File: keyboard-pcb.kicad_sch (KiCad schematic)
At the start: 0 parts

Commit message: added stm32
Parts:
- added D1: PRTR5V0U2X, Package_TO_SOT_SMD:SOT-143, symbol Power_Protection:PRTR5V0U2X
- added J1: USB_C_Receptacle_USB2.0_14P, symbol Connector:USB_C_Receptacle_USB2.0_14P
- added R1, R2: 5.1k, symbol Device:R_Small_US
- added U1: STM32F072CBTx, Package_QFP:LQFP-48_7x7mm_P0.5mm, symbol MCU_ST_STM32F0:STM32F072CBTx
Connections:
- new net: J1.A4 (VBUS), J1.A9 (VBUS), J1.B4 (VBUS), J1.B9 (VBUS)
- new net: J1.A5 (CC1), R2.1
- new net: J1.B5 (CC2), R1.2
- new net +3V3: U1.1 (VBAT), U1.24 (VDD), U1.36 (VDDIO2), U1.48 (VDD), U1.9 (VDDA)
- new net GND: J1.A1 (GND), J1.A12 (GND), J1.B1 (GND), J1.B12 (GND), J1.SH (SHIELD), R1.1, R2.2, U1.23 (VSS), U1.35 (VSS), U1.47 (VSS), U1.8 (VSSA)
- new net USB_D+: J1.A6 (D+), J1.B6 (D+), U1.33 (PA12)
- new net USB_D-: J1.A7 (D-), J1.B7 (D-), U1.32 (PA11)

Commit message: added libraries
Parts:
- removed D1: PRTR5V0U2X, Package_TO_SOT_SMD:SOT-143, symbol Power_Protection:PRTR5V0U2X
- added C1, C2, C3, C4, C5: 0.1uF, symbol Device:C_Small
- added C6, C7, C8: 1uF, symbol Device:C_Small
- added D1: D5V0F1U2LP-7B, Diode_SMD:D_0402_1005Metric_Pad0.77x0.64mm_HandSolder, symbol Device:D_TVS
- added D2: PRTR5V0U2X, Package_TO_SOT_SMD:SOT-143, symbol Power_Protection:PRTR5V0U2X
- added D4: BZT52C5V1-7-F, Diode_SMD:D_SOD-123, symbol Device:D_Zener
- added U2: XC6206PxxxMR, Package_TO_SOT_SMD:SOT-23-3, symbol Regulator_Linear:XC6206PxxxMR
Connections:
- net +3V3: now also C1.1, C2.1, C3.1, C4.1, C5.1, C6.1, C8.1, U2.2 (VO)
- net GND: now also C1.2, C2.2, C3.2, C4.2, C5.2, C6.2, C7.2, C8.2, D1.1 (A1), D2.1 (GND), U2.1 (GND)
- net at J1.A4 (VBUS), J1.A9 (VBUS), J1.B4 (VBUS)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: now also D1.2 (A2), D4.2 (A)
- net USB_D+ renamed D+
- net D+: now also D2.3 (I/O2)
- net USB_D- renamed D-
- net D-: now also D2.2 (I/O1)
- new net +5V: C7.1, D2.4 (VCC), D4.1 (K), U2.3 (VI)
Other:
- note added: "Decoupling Capacitors"
- note added: "MCU"
- note added: "USB Port"
- moved on the sheet: J1, R1, R2

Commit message: finished rest of the schematic
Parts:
- removed D1: D5V0F1U2LP-7B, Diode_SMD:D_0402_1005Metric_Pad0.77x0.64mm_HandSolder, symbol Device:D_TVS
- removed D4: BZT52C5V1-7-F, Diode_SMD:D_SOD-123, symbol Device:D_Zener
- added C9: 0.1uF, symbol Device:C_Small
- added F1: 500mA, symbol Device:Polyfuse
- added J4: Conn_01x05, symbol Connector_Generic:Conn_01x05
- added R3, R4: 5.1k, symbol Device:R_Small_US
- added SW1, SW2: RESET, symbol Switch:SW_Push
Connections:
- net +3V3: now also J4.5 (Pin_5), SW2.1
- net +5V: now also F1.2; no longer D2.4 (VCC)
- net GND: now also C9.2, J4.1 (Pin_1), R4.1, SW1.2
- net VBUS: now reaches J1.A4 (VBUS), J1.A9 (VBUS), J1.B4 (VBUS), J1.B9 (VBUS)
- net VBUS: now also D2.4 (VCC), F1.1
- net CLK: now reaches U1.34 (PA13)
- net DATA: now reaches U1.37 (PA14)
- net BOOT: now reaches U1.44 (BOOT0)
- net BOOT: now also R3.2, SW2.2
- net NRST: now reaches U1.7 (NRST)
- net NRST: now also C9.1, SW1.1
- new net: R3.1, R4.2
- new net RST: J4.4 (Pin_4)
- new net SWCLK: J4.3 (Pin_3)
- new net SWDIO: J4.2 (Pin_2)
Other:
- added sheet Keyboard Matrix (keyboard-matrix.kicad_sch)
- note added: "Boot and Reset switches"
- note added: "Debug"
- note added: "ESD Protection"
- note added: "LDO"
- note added: "USB-C Port"
- note removed: "USB Port"
- title: (none) -> AwesomeKey
- moved on the sheet: C1, C2, C3, C4, C5, C6, C7, C8, D2, J1, R1, R2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

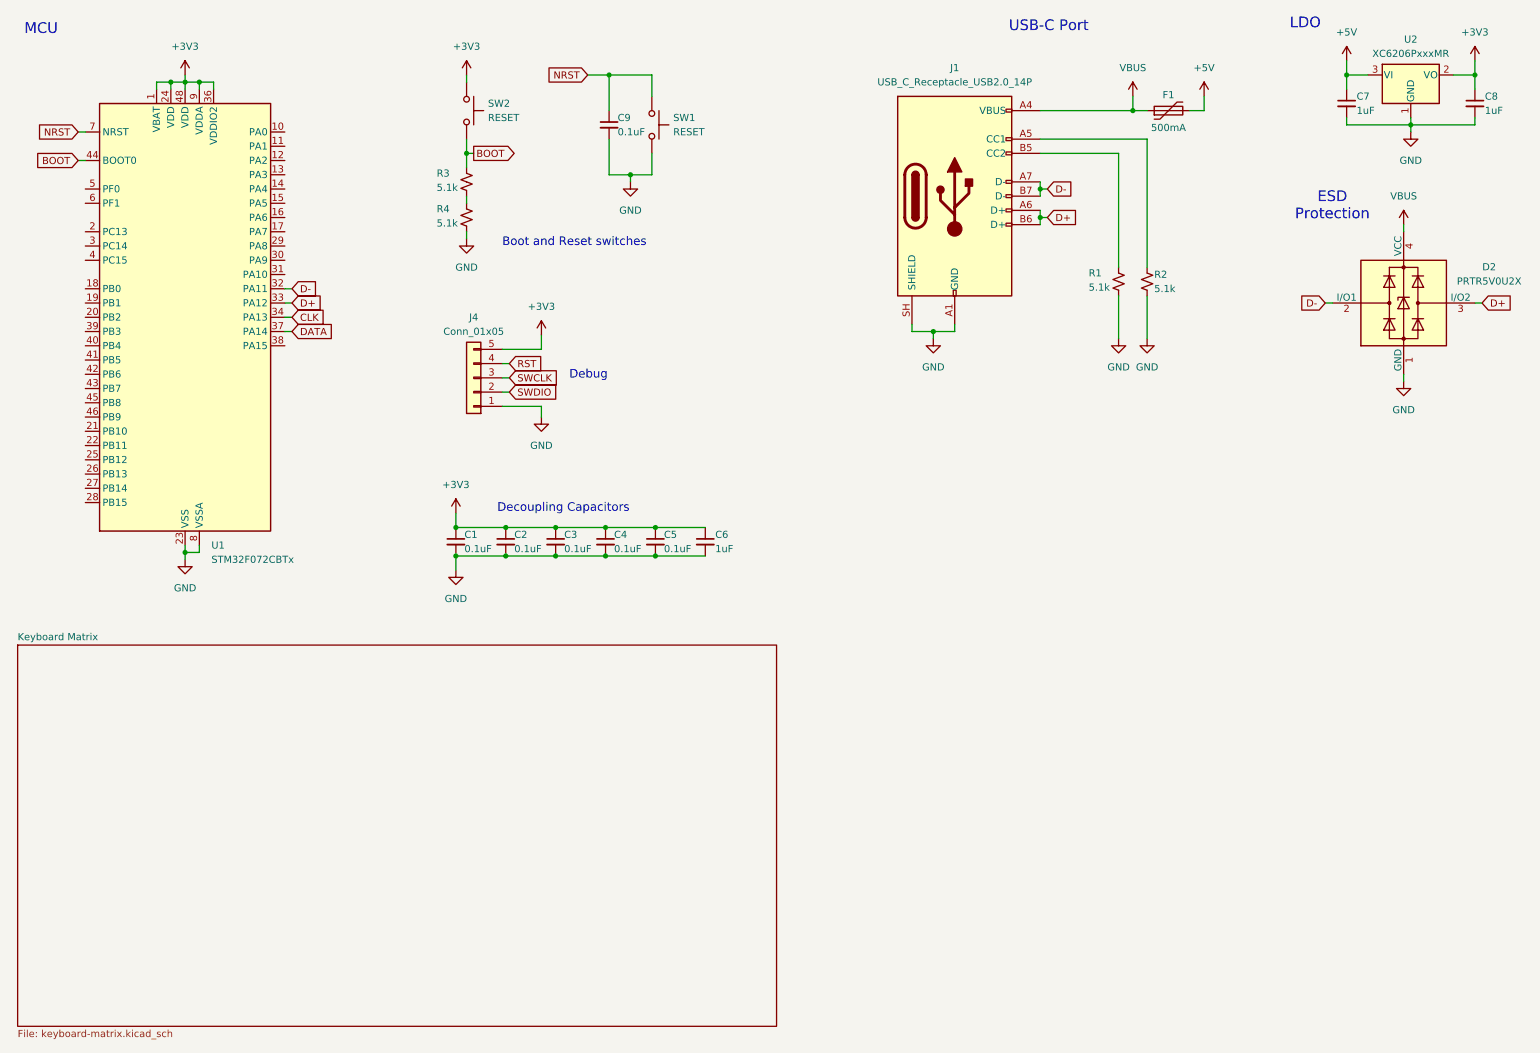
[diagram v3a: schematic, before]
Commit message: added led matrix for backlight
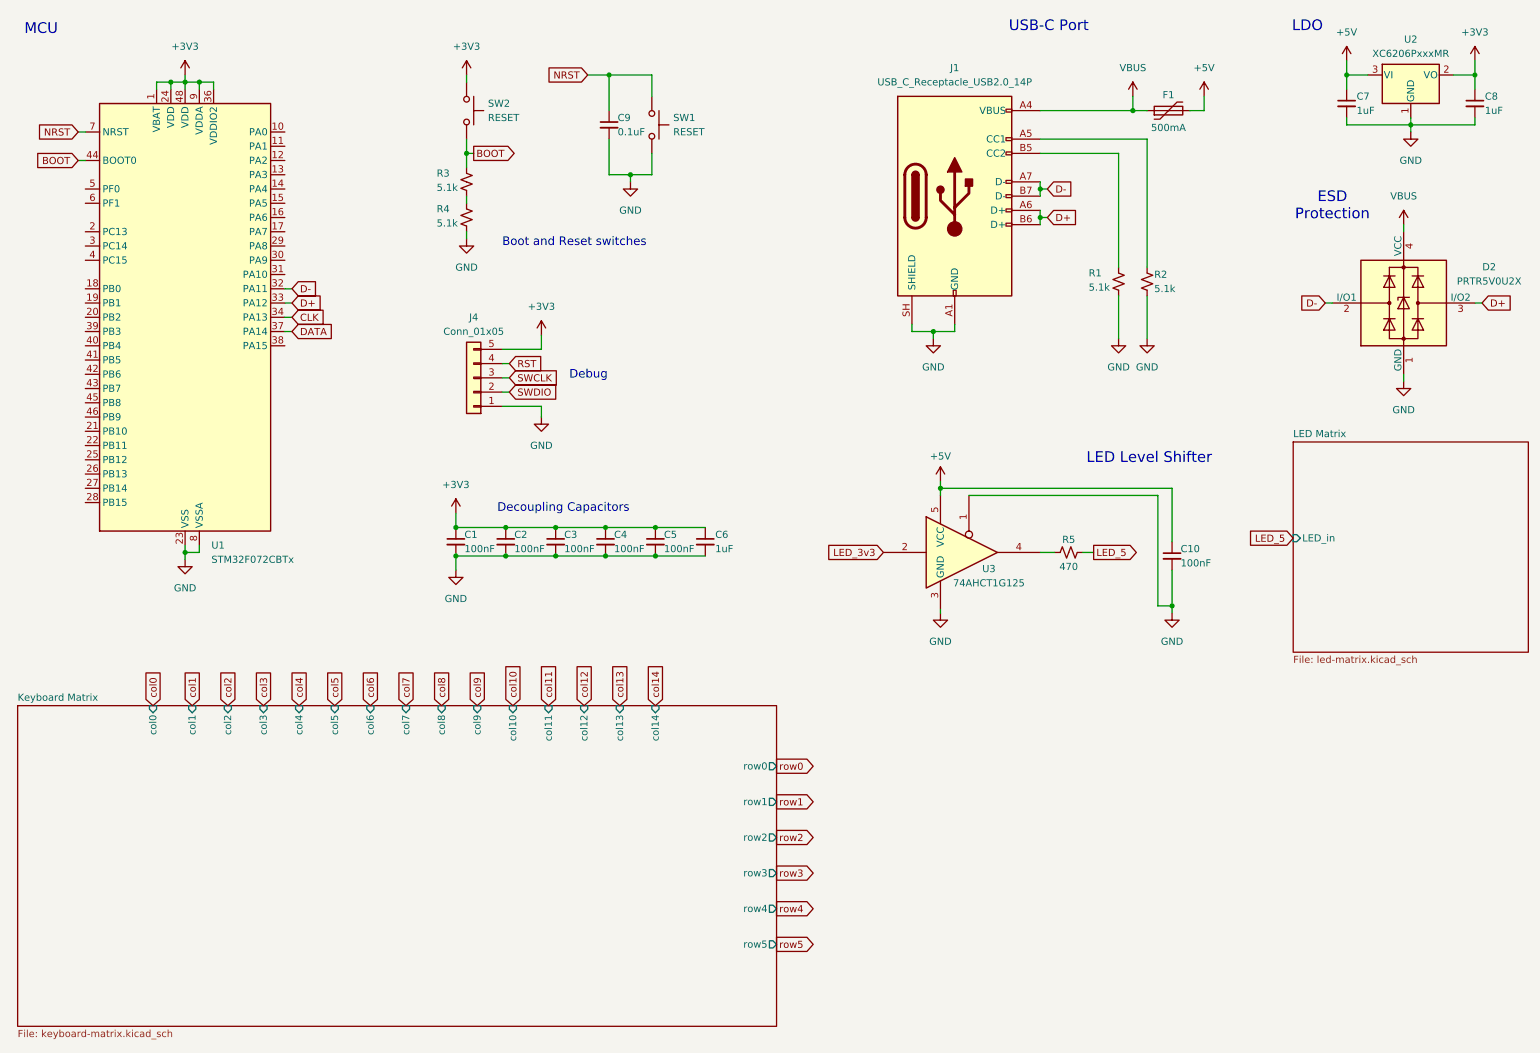
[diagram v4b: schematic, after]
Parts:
- added C10: 100nF, symbol Device:C_Small
- added R5: 470, symbol Device:R_Small_US
- added U3: 74AHCT1G125, symbol 74xGxx:74AHCT1G125
- C1, C2, C3, C4, C5: value 0.1uF -> 100nF
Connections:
- net +5V: now also C10.1, U3.5 (VCC)
- net GND: now also C10.2, U3.1, U3.3 (GND)
- new net: R5.1, U3.4
- new net LED_3v3: U3.2
- new net LED_5: R5.2
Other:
- added sheet LED Matrix (led-matrix.kicad_sch)
- sheet Keyboard Matrix ports: added col0, col1, col10, col11, col12, col13, col14, col2, col3, col4, col5, col6, col7, col8, col9, row0, row1, row2, row3, row4, row5; removed none
- note added: "LED Level Shifter"

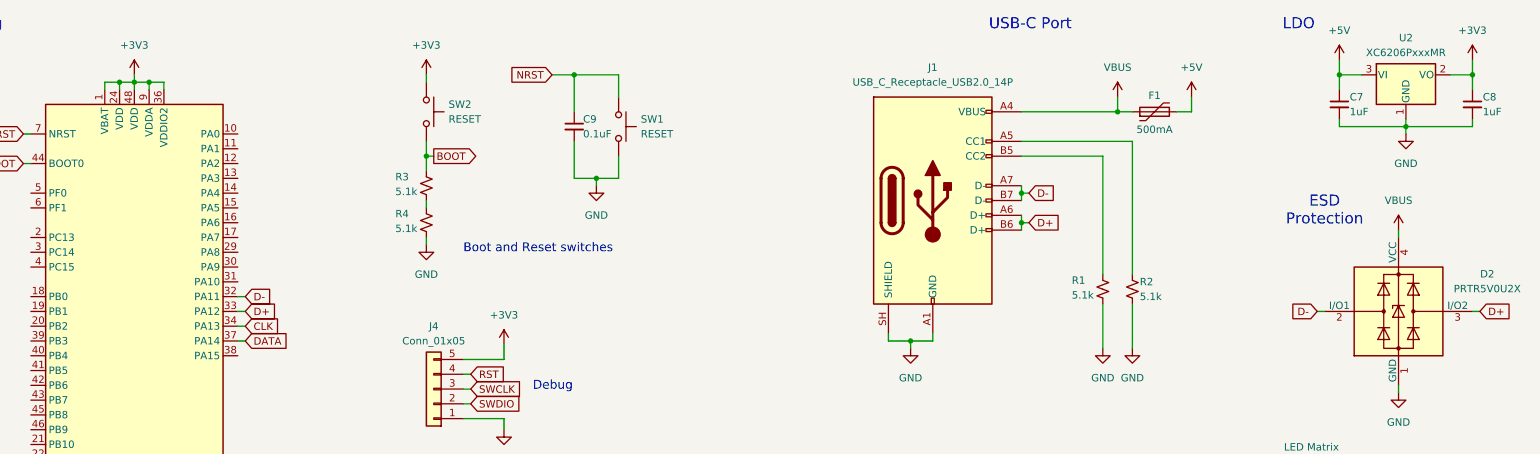
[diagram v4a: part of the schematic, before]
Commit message: assigned footprints
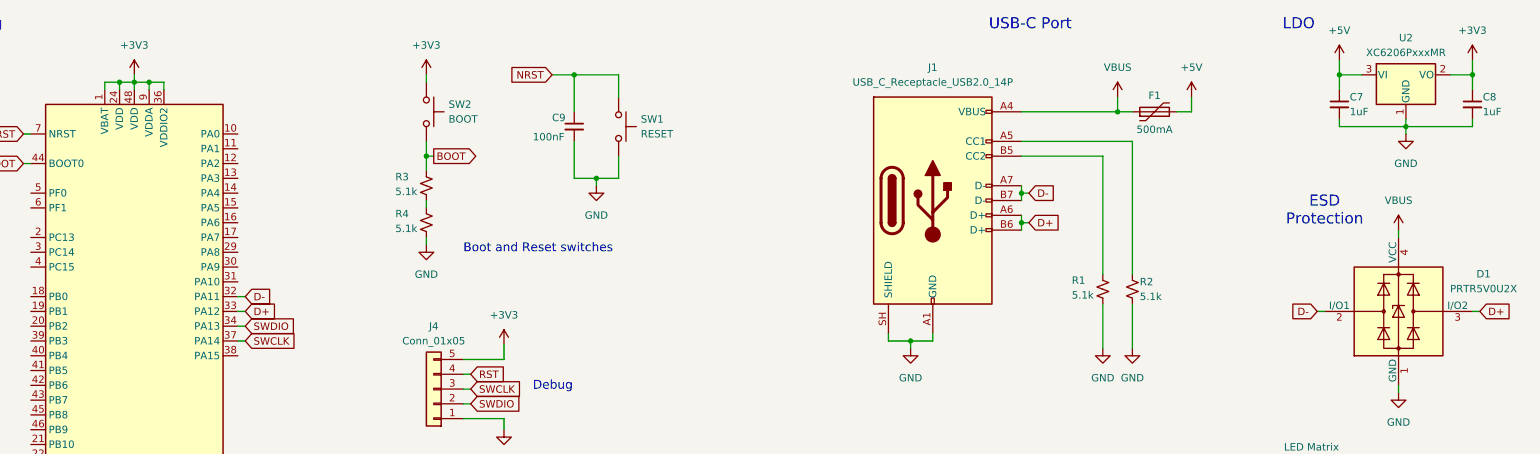
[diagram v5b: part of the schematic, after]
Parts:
- C1, C10, C2, C3, C4, C5: footprint (none) -> Capacitor_SMD:C_0402_1005Metric
- C6, C7, C8: footprint (none) -> Capacitor_SMD:C_0603_1608Metric
- C9: value 0.1uF -> 100nF; footprint (none) -> Capacitor_SMD:C_0402_1005Metric
- F1: footprint (none) -> Fuse:Fuse_1206_3216Metric
- J1: footprint (none) -> PCM_marbastlib-various:USB_C_Receptacle_HRO_TYPE-C-31-M-12
- J4: footprint (none) -> Connector_PinHeader_2.54mm:PinHeader_1x05_P2.54mm_Vertical
- R1, R2, R3, R4, R5: footprint (none) -> Resistor_SMD:R_0402_1005Metric
- SW1: footprint (none) -> Button_Switch_SMD:SW_SPST_TL3342
- SW2: value RESET -> BOOT; footprint (none) -> Button_Switch_SMD:SW_SPST_TL3342
- U3: footprint (none) -> Package_TO_SOT_SMD:SOT-23-5
- renumbered D2 to D1
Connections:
- net CLK is gone; now on net SWDIO: U1.34 (PA13)
- net DATA is gone; now on net SWCLK: U1.37 (PA14)
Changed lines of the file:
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@@
 	)
 	(junction
-		(at 41.275 26.67)
-		(diameter 0)
-		(color 0 0 0 0)
-	)
-	(junction
 		(at 177.165 71.12)
 		(diameter 0)
@@
 	)
 	(junction
+		(at 41.275 26.67)
+		(diameter 0)
+		(color 0 0 0 0)
+	)
+	(junction
 		(at 127.635 106.045)
 		(diameter 0)
@@
 	(wire
 		(pts
+			(xy 38.735 26.67) (xy 38.735 27.94)
+		)
+		(stroke
+			(width 0)
+			(type default)
+		)
+	)
+	(wire
+		(pts
 			(xy 93.98 39.37) (xy 95.25 39.37)
 		)
@@
 	(wire
 		(pts
-			(xy 38.735 27.94) (xy 38.735 26.67)
-		)
-		(stroke
-			(width 0)
-			(type default)
-		)
-	)
-	(wire
-		(pts
 			(xy 48.895 26.67) (xy 46.355 26.67)
 		)
@@
 		)
 	)
-	(global_label "CLK"
+	(global_label "SWCLK"
 		(shape input)
-		(at 62.865 68.58 0)
+		(at 62.865 71.12 0)
 		(fields_autoplaced yes)
 		(effects
@@
 		)
 		(property "Intersheetrefs" "${INTERSHEET_REFS}"
-			(at 69.4183 68.58 0)
+			(at 72.0792 71.12 0)
 			(hide yes)
 			(show_name no)
@@
 		)
 	)
-	(global_label "DATA"
+	(global_label "SWDIO"
 		(shape input)
-		(at 62.865 71.12 0)
+		(at 62.865 68.58 0)
 		(fields_autoplaced yes)
 		(effects
@@
 		)
 		(property "Intersheetrefs" "${INTERSHEET_REFS}"
-			(at 70.265 71.12 0)
+			(at 71.7164 68.58 0)
 			(hide yes)
 			(show_name no)
@@
 			)
 		)
-		(property "Footprint" ""
+		(property "Footprint" "PCM_marbastlib-various:USB_C_Receptacle_HRO_TYPE-C-31-M-12"
 			(at 184.785 46.99 0)
 			(hide yes)
@@
 			)
 		)
-		(property "Footprint" ""
+		(property "Footprint" "Resistor_SMD:R_0402_1005Metric"
 			(at 215.265 62.23 0)
 			(hide yes)
@@
 			)
 		)
-		(property "Footprint" ""
+		(property "Footprint" "Capacitor_SMD:C_0603_1608Metric"
 			(at 250.825 30.48 0)
 			(hide yes)
@@
 		(dnp no)
 		(property "Reference" "C9"
-			(at 120.904 33.02 0)
+			(at 115.57 32.766 0)
 			(show_name no)
 			(do_not_autoplace no)
@@
 			)
 		)
-		(property "Value" "0.1uF"
-			(at 120.904 35.56 0)
+		(property "Value" "100nF"
+			(at 112.268 36.068 0)
 			(show_name no)
 			(do_not_autoplace no)
@@
 			)
 		)
-		(property "Footprint" ""
+		(property "Footprint" "Capacitor_SMD:C_0402_1005Metric"
 			(at 119.38 34.29 0)
 			(hide yes)
@@
 			)
 		)
-		(property "Value" "RESET"
+		(property "Value" "BOOT"
 			(at 97.79 33.0199 90)
 			(show_name no)
@@
 			)
 		)
-		(property "Footprint" ""
+		(property "Footprint" "Button_Switch_SMD:SW_SPST_TL3342"
 			(at 99.06 31.75 0)
 			(hide yes)
@@
 			)
 		)
-		(property "Footprint" ""
+		(property "Footprint" "Fuse:Fuse_1206_3216Metric"
 			(at 224.155 30.48 0)
 			(hide yes)
@@
 			)
 		)
-		(property "Footprint" ""
+		(property "Footprint" "Resistor_SMD:R_0402_1005Metric"
 			(at 210.185 62.23 0)
 			(hide yes)
@@
 			)
 		)
-		(property "Footprint" ""
+		(property "Footprint" "Resistor_SMD:R_0402_1005Metric"
 			(at 201.295 110.49 0)
 			(hide yes)
@@
 			)
 		)
-		(property "Footprint" ""
+		(property "Footprint" "Resistor_SMD:R_0402_1005Metric"
 			(at 93.98 44.45 0)
 			(hide yes)
@@
 			)
 		)
-		(property "Footprint" ""
+		(property "Footprint" "Capacitor_SMD:C_0402_1005Metric"
 			(at 109.855 108.585 0)
 			(hide yes)
@@
 			)
 		)
-		(property "Footprint" ""
+		(property "Footprint" "Package_TO_SOT_SMD:SOT-23-5"
 			(at 183.515 110.49 0)
 			(hide yes)
@@
 			)
 		)
-		(property "Footprint" ""
+		(property "Footprint" "Capacitor_SMD:C_0402_1005Metric"
 			(at 118.745 108.585 0)
 			(hide yes)
@@
 			)
 		)
-		(property "Footprint" ""
+		(property "Footprint" "Connector_PinHeader_2.54mm:PinHeader_1x05_P2.54mm_Vertical"
 			(at 95.25 79.375 0)
 			(hide yes)
@@
 			)
 		)
-		(property "Footprint" ""
+		(property "Footprint" "Button_Switch_SMD:SW_SPST_TL3342"
 			(at 132.08 34.29 0)
 			(hide yes)
@@
 			)
 		)
-		(property "Footprint" ""
+		(property "Footprint" "Capacitor_SMD:C_0603_1608Metric"
 			(at 273.685 30.48 0)
 			(hide yes)
@@
 			)
 		)
-		(property "Footprint" ""
+		(property "Footprint" "Capacitor_SMD:C_0603_1608Metric"
 			(at 136.525 108.585 0)
 			(hide yes)
@@
 			)
 		)
-		(property "Footprint" ""
+		(property "Footprint" "Capacitor_SMD:C_0402_1005Metric"
 			(at 127.635 108.585 0)
 			(hide yes)
@@
 			)
 		)
-		(property "Footprint" ""
+		(property "Footprint" "Capacitor_SMD:C_0402_1005Metric"
 			(at 219.71 111.125 0)
 			(hide yes)
@@
 		(dnp no)
 		(fields_autoplaced yes)
-		(property "Reference" "D2"
-			(at 276.225 59.6198 0)
+		(property "Reference" "D1"
+			(at 275.59 59.6198 0)
 			(show_name no)
 			(do_not_autoplace no)
@@
 		)
 		(property "Value" "PRTR5V0U2X"
-			(at 276.225 62.1598 0)
+			(at 275.59 62.1598 0)
 			(show_name no)
 			(do_not_autoplace no)
@@
 			(project "keyboard-pcb"
 				(path "/a41dad29-4328-40a3-b427-6ea31b74fde8"
-					(reference "D2")
+					(reference "D1")
 					(unit 1)
 				)
@@
 			)
 		)
-		(property "Footprint" ""
+		(property "Footprint" "Capacitor_SMD:C_0402_1005Metric"
 			(at 100.965 108.585 0)
 			(hide yes)
@@
 			)
 		)
-		(property "Footprint" ""
+		(property "Footprint" "Capacitor_SMD:C_0402_1005Metric"
 			(at 92.075 108.585 0)
 			(hide yes)
@@
 			)
 		)
-		(property "Footprint" ""
+		(property "Footprint" "Resistor_SMD:R_0402_1005Metric"
 			(at 93.98 50.8 0)
 			(hide yes)

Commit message: routed switch matrix
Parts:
- removed J1: USB_C_Receptacle_USB2.0_14P, PCM_marbastlib-various:USB_C_Receptacle_HRO_TYPE-C-31-M-12, symbol Connector:USB_C_Receptacle_USB2.0_14P
- added J2: USB_C_Receptacle_USB2.0_16P, PCM_marbastlib-various:USB_C_Receptacle_HRO_TYPE-C-31-M-12, symbol Connector:USB_C_Receptacle_USB2.0_16P
- renumbered C1 to C85, C2 to C86, C3 to C87, C4 to C88, C5 to C89, C6 to C90, C9 to C91, C7 to C92, C8 to C93, C10 to C94, J4 to J1, R3 to R1, R4 to R2, R5 to R3, R1 to R4, R2 to R5, SW2 to SW1, SW1 to SW2, U3 to U2, U2 to U3
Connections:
- net D+: now also J2.A6 (D+), J2.B6 (D+)
- net D-: now also J2.A7 (D-), J2.B7 (D-)
- net GND: now also J2.A1 (GND), J2.A12 (GND), J2.B1 (GND), J2.B12 (GND), J2.SH (SHIELD)
- net VBUS: now also J2.A4 (VBUS), J2.A9 (VBUS), J2.B4 (VBUS), J2.B9 (VBUS)
- net col0: now also U1.38 (PA15)
- net col1: now also U1.39 (PB3)
- net col10: now also U1.27 (PB14)
- net col11: now also U1.28 (PB15)
- net col12: now also U1.29 (PA8)
- net col13: now also U1.30 (PA9)
- net col14: now also U1.31 (PA10)
- net col2: now also U1.40 (PB4)
- net col3: now also U1.41 (PB5)
- net col4: now also U1.42 (PB6)
- net col5: now also U1.43 (PB7)
- net col6: now also U1.13 (PA3)
- net col7: now also U1.14 (PA4)
- net col8: now also U1.25 (PB12)
- net col9: now also U1.26 (PB13)
- net at R5.1: now also J2.A5 (CC1)
- net at R4.2: now also J2.B5 (CC2)
- no-connect marks 0 -> 2
